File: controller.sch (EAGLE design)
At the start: 47 parts, among them IC1 7805DT, Q1 MOSFET_PCHANNEL, Q2 MOSFET-NCHANNELBSS123LT1G, Q3 MOSFET-NCHANNELFDD8780, U1 ATMEGA328P, Y1 16MHz

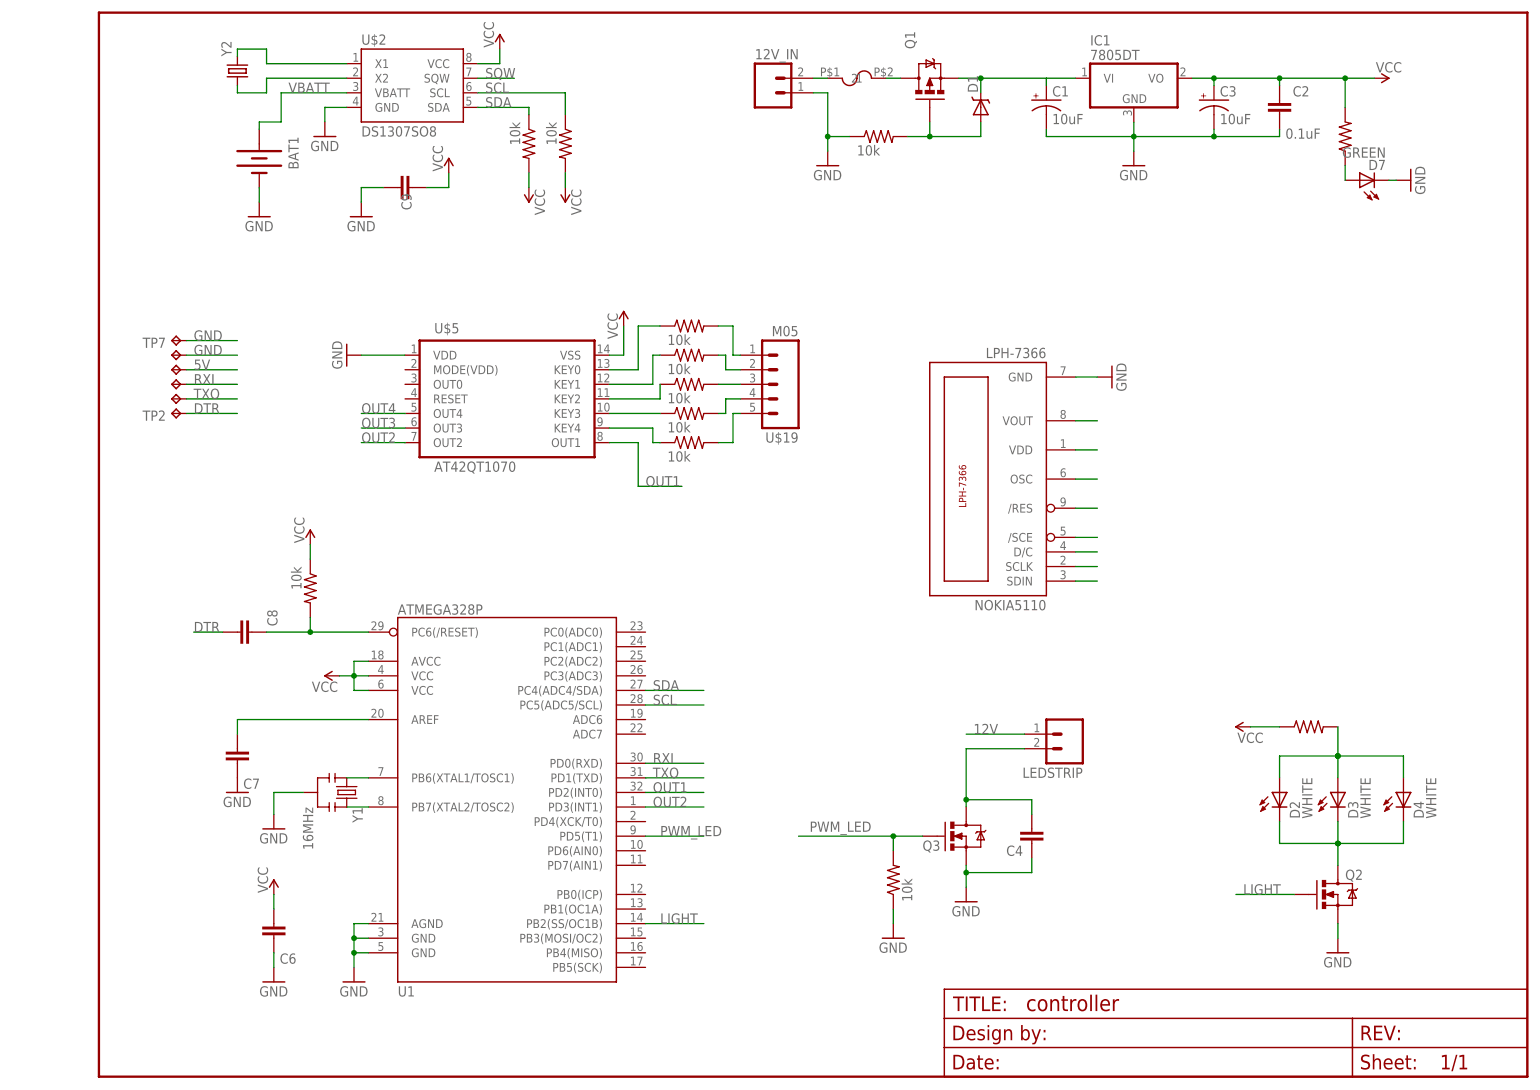
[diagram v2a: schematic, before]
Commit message: decreased board size
add backlight leds. changed to locking through hole programming header.
reorganized and tightened voltage regulator section.
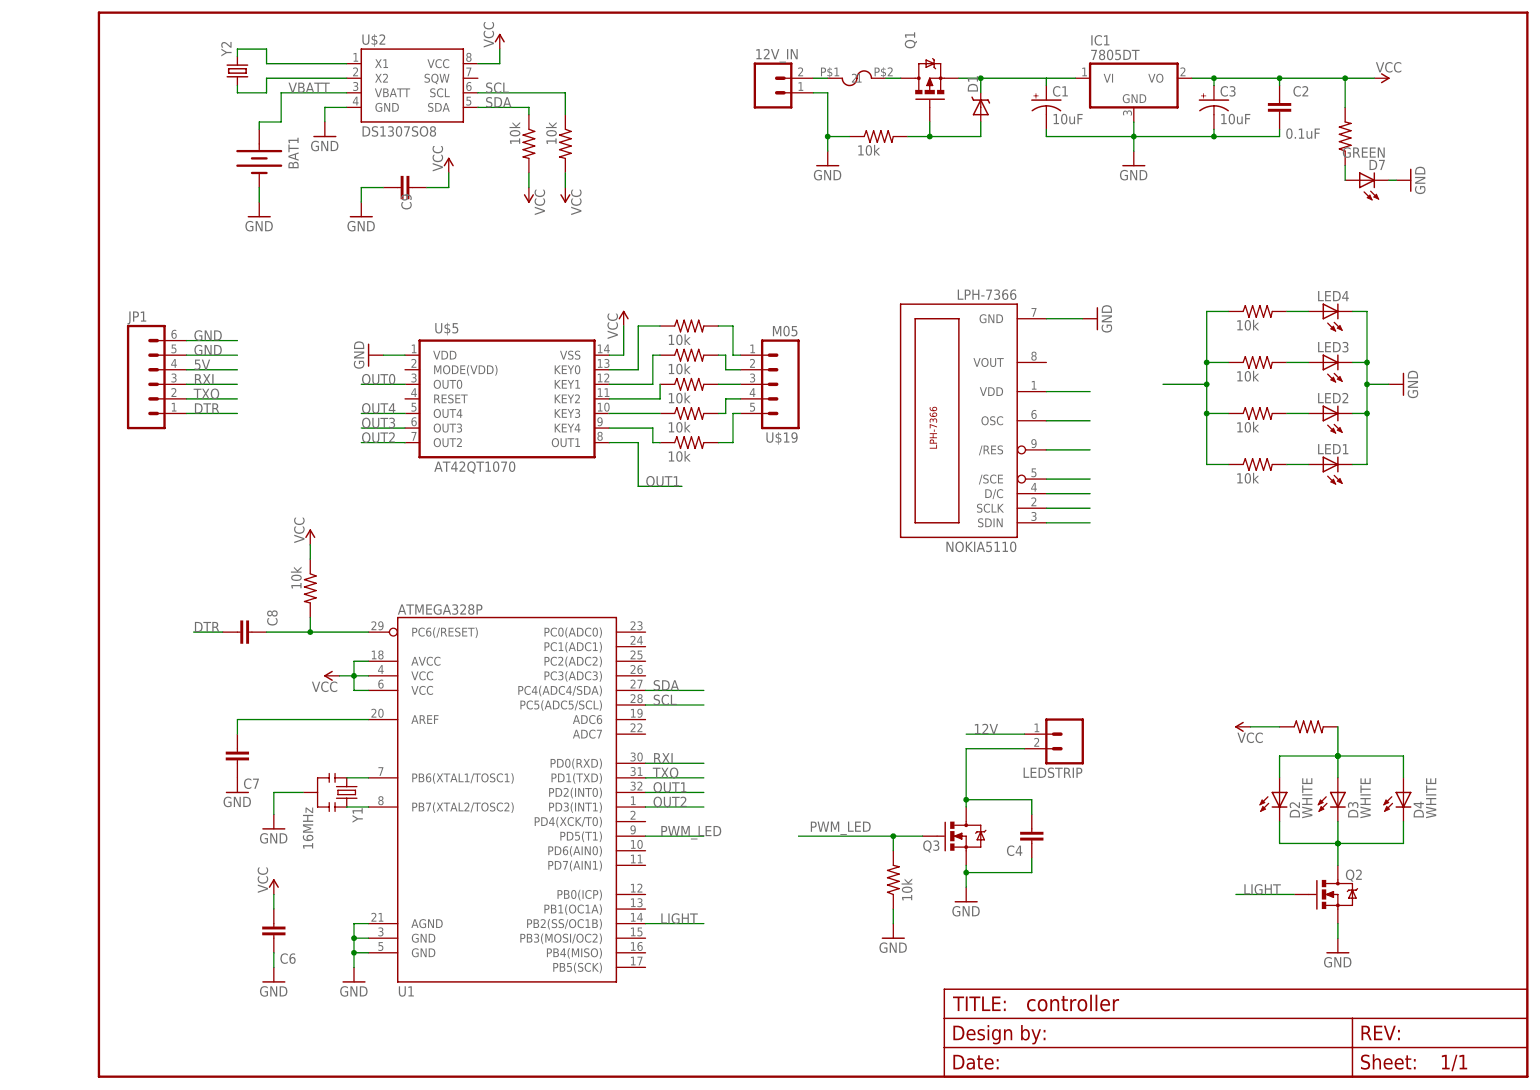
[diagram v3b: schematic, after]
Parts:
- removed TP2, TP3, TP4, TP5, TP6, TP7: TPTP12SQ, testpad:TPTP12SQ
- added JP1: (no value), SparkFun-Connectors:M06LOCK
- added LED1, LED2, LED3, LED4: (no value), SparkFun-LED:LED0603
- added U$18, U$21, U$22, U$6: 10k, jt_parts:RESISTOR
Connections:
- removed net SQW: U$2.SQW
- new net N$33: LED3.A, U$18.2
- new net N$34: LED2.A, U$21.2
- new net N$35: LED1.A, U$22.2
- new net N$39: U$18.1, U$21.1, U$22.1, U$6.1
- new net OUT0: U$5.OUT0
- net 5V: now also JP1.4; no longer TP5.TP
- net DTR: now also JP1.1; no longer TP2.TP
- net GND: now also JP1.5, JP1.6, LED1.C, LED2.C, LED3.C, LED4.C; no longer TP6.TP, TP7.TP
- net N$22: now also LED4.A, U$6.2; no longer NOKIA5110.VOUT
- net RXI: now also JP1.3; no longer TP4.TP
- net TXO: now also JP1.2; no longer TP3.TP
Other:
- moved on the sheet: NOKIA5110

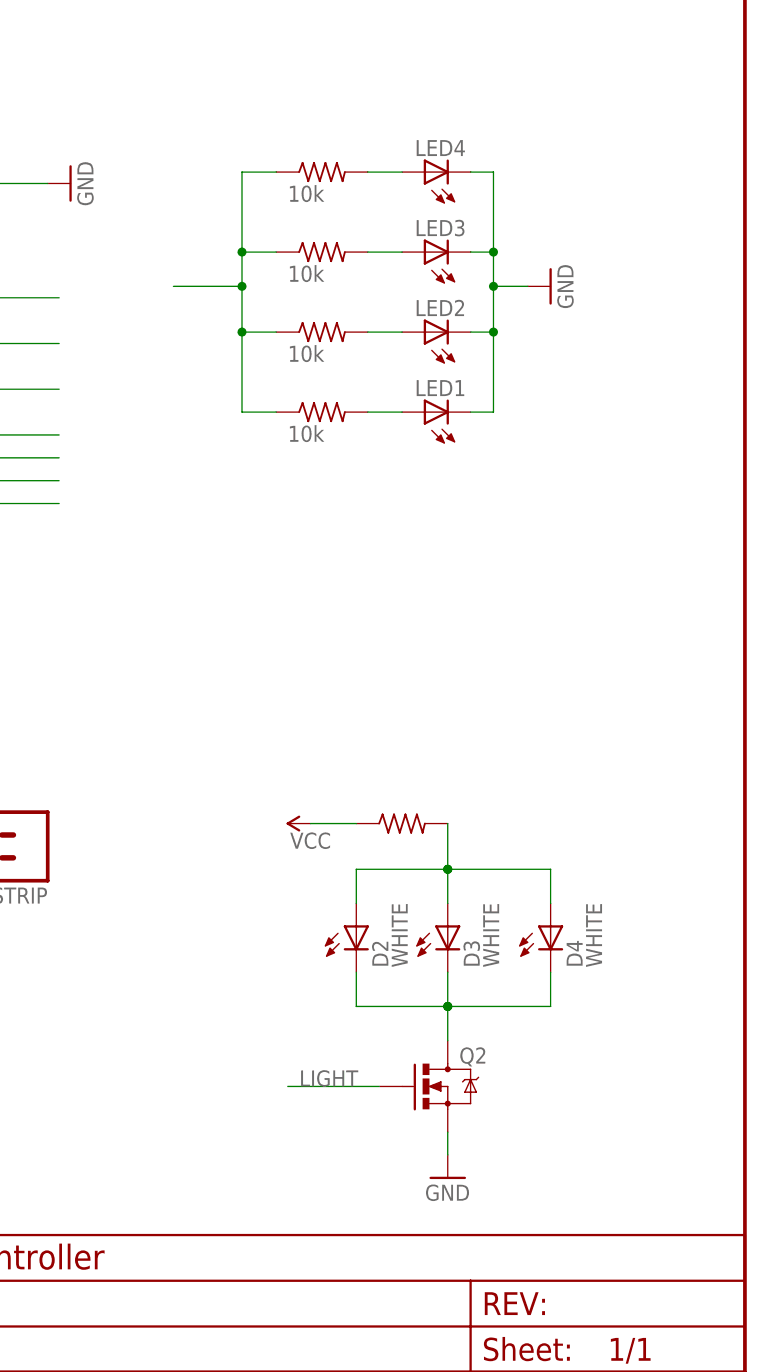
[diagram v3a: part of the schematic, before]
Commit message: added current limit resistors. tightened rtc-mcu spacing.
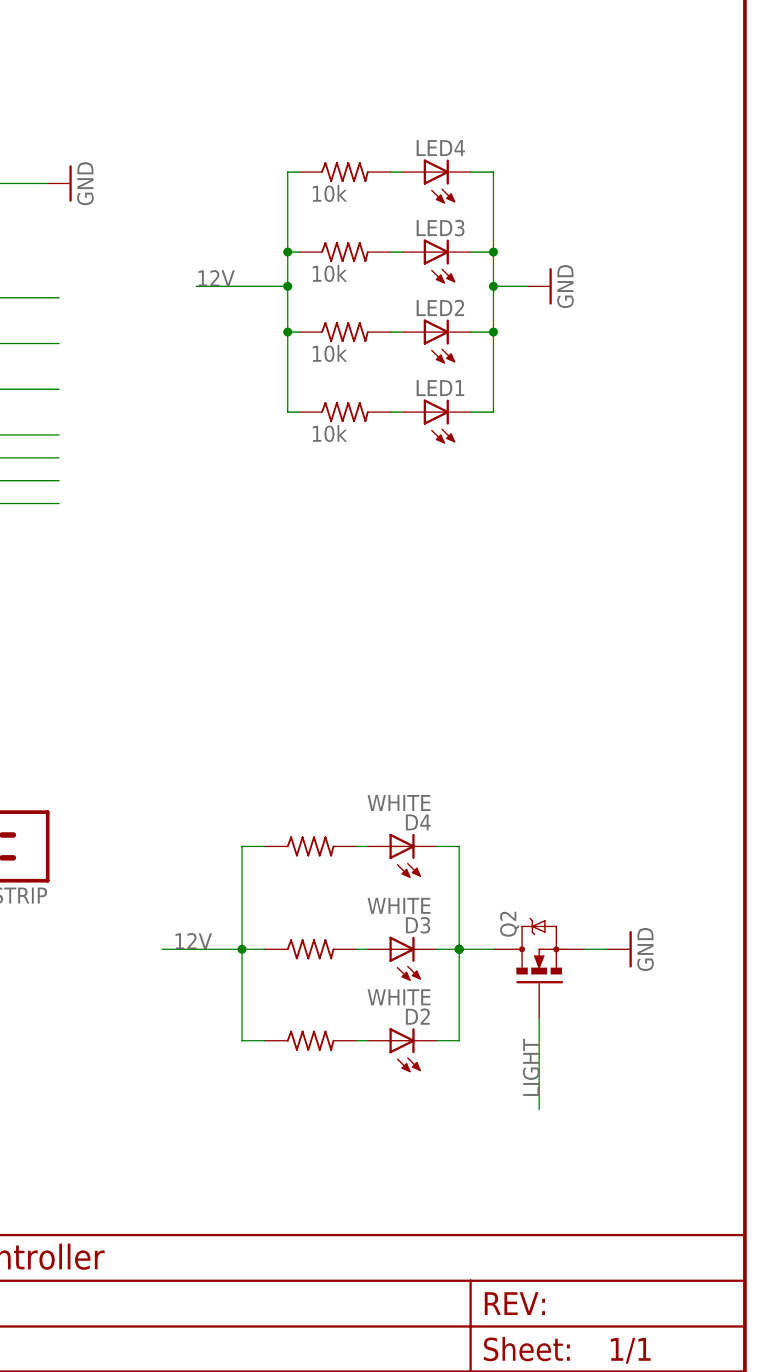
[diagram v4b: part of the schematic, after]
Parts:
- added U$23, U$24: (no value), jt_parts:RESISTOR
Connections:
- removed net N$39: U$18.1, U$21.1, U$22.1, U$6.1
- new net N$36: D2.A, U$24.2
- new net N$37: D4.A, U$23.2
- net 12V: now also U$18.1, U$21.1, U$22.1, U$23.1, U$24.1, U$3.1, U$6.1
- net 5V: no longer U$3.1
- net N$9: no longer D2.A, D4.A
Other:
- moved on the sheet: D2, D3, D4, Q2

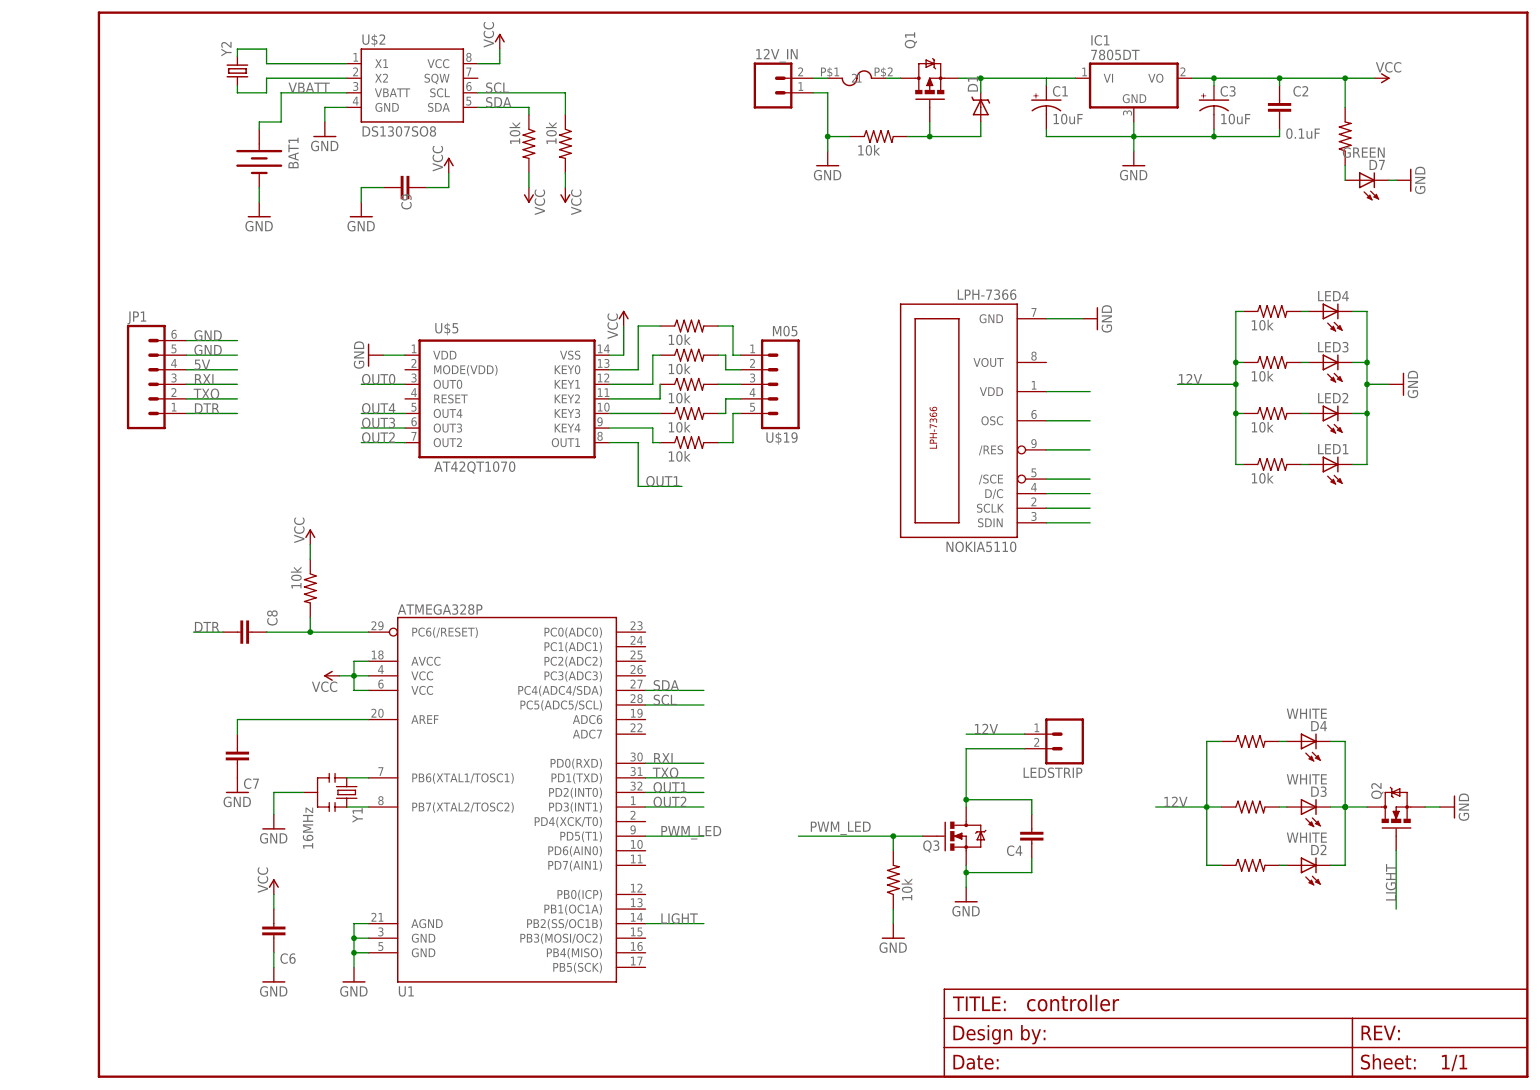
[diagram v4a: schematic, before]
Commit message: wired lcd for software reset.
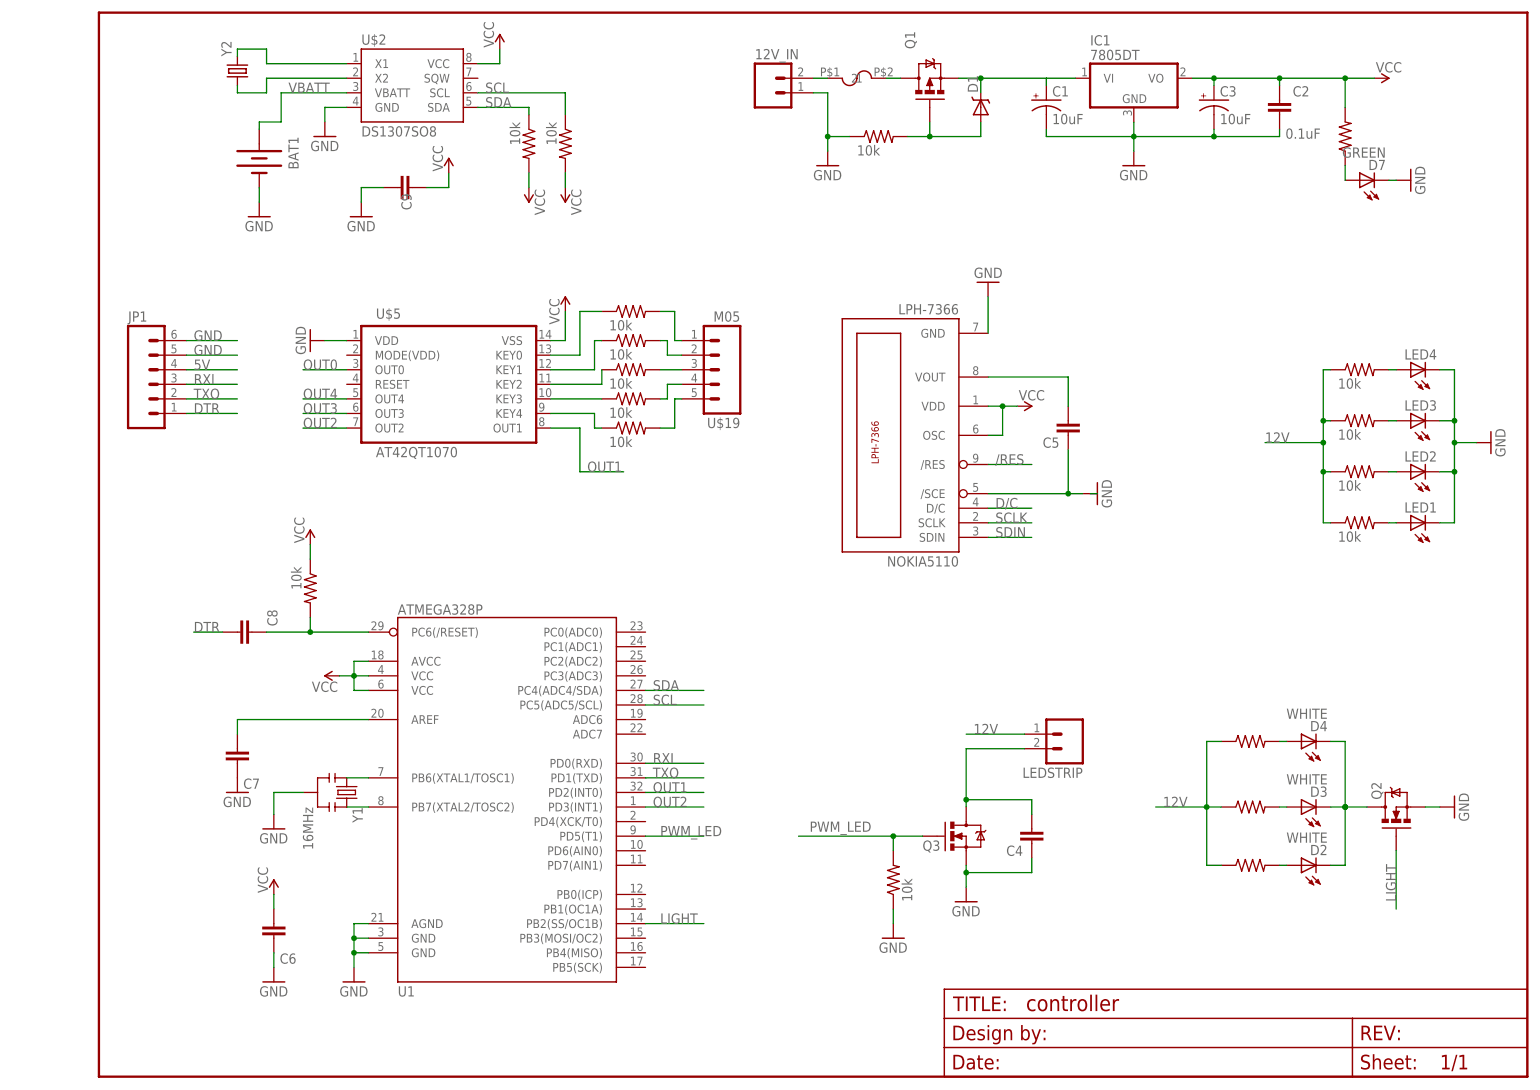
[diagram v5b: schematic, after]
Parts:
- added C5: (no value), SparkFun-Capacitors:CAP0805
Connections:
- net N$17 renamed D/C
- net N$19 renamed /RES
- net N$2 renamed SDIN
- net N$5 renamed SCLK
- removed net N$18: NOKIA5110./SCE
- new net VCC: NOKIA5110.OSC, NOKIA5110.VDD, U$10.2, U$9.2
- net 5V: no longer NOKIA5110.VDD, U$10.2, U$9.2
- net GND: now also C5.1, NOKIA5110./SCE
- net N$20: now also C5.2, NOKIA5110.VOUT; no longer NOKIA5110.OSC
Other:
- moved on the sheet: LED1, LED2, LED3, LED4, NOKIA5110, U$19, U$5

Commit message: added sideview led footprint and replaced for night lights.
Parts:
- D2, D3, D4: device adafruit:LEDMICRO-SIDELED -> jt_parts:LED
- JP1: device SparkFun-Connectors:M06LOCK -> SparkFun-Connectors:M06POGOPIN_HOLES_ONLY
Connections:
- net 12V: no longer U$18.1, U$21.1, U$22.1, U$23.1, U$24.1, U$3.1, U$6.1
- net 5V: now also U$18.1, U$21.1, U$22.1, U$23.1, U$24.1, U$3.1, U$6.1
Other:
- note added: "Night Light"
